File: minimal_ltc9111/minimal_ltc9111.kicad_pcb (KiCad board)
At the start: 4 copper layers, 62.2 x 19 mm, 35 parts, among them J1 FW-02-03-G-D-085-155, J2 FW-02-03-G-D-085-155, Q1 100 V, Q2 100 V, Q3 100 V, Q4 100.0 V, U1 LTC9111RDE-PBF

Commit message: Update subproject commit and correct component values in minimal_ltc9111.kicad_sch
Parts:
- L1: value 68 µH -> 68.0 µH

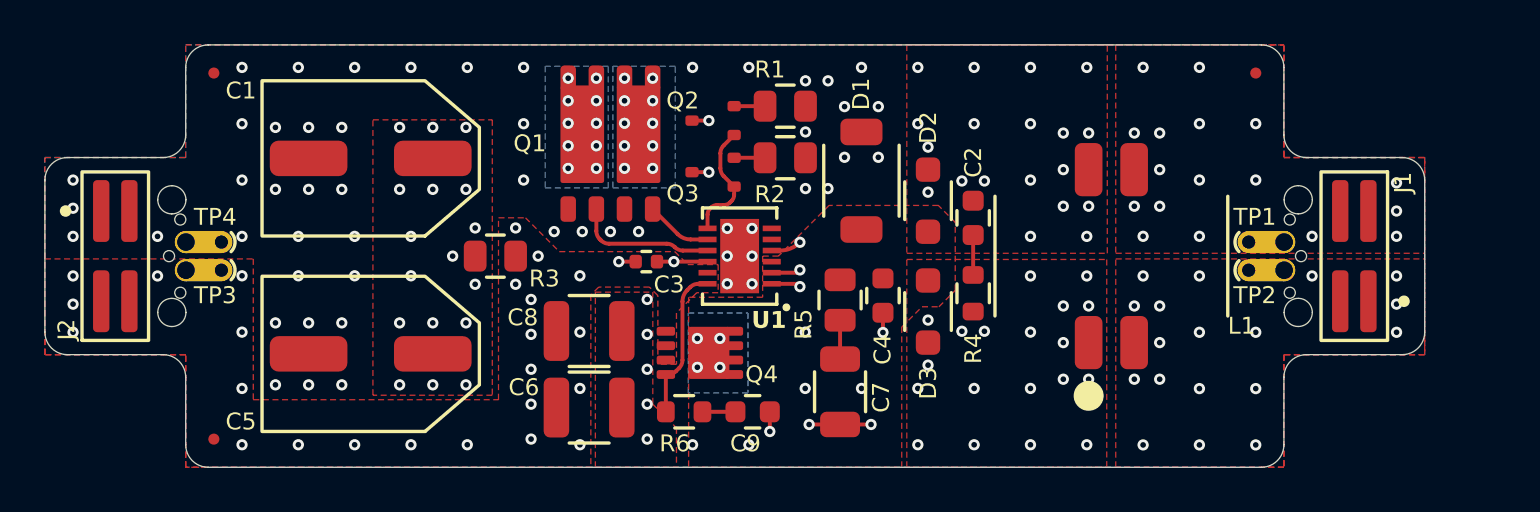
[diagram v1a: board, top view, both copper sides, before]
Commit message: Update subproject commit in KiCAD_Symbol_Generator
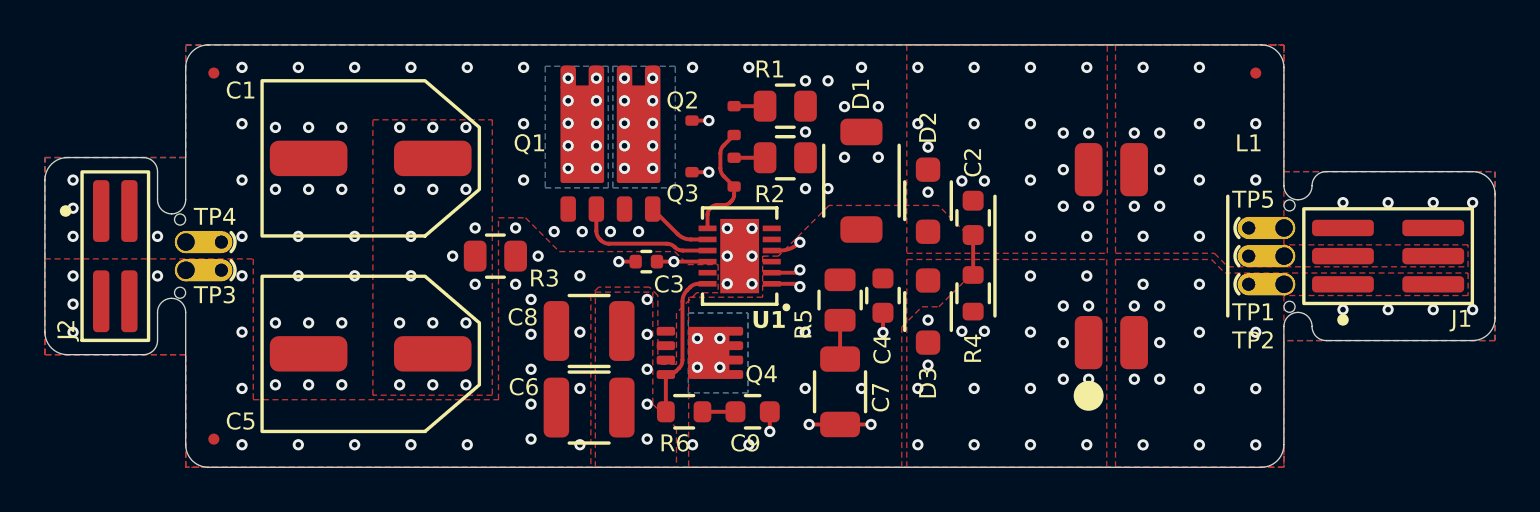
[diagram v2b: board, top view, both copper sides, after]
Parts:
- added TP5: TestPoint, test_point_footprints:TestPoint_THTPad_Castelated, F.Cu at (179.1, 103.9)
- J1: value FW-02-03-G-D-085-155 -> FW-03-03-G-D-085-155; footprint connector_footprints:FW-02-03-G-D-085-155 -> connector_footprints:FW-03-03-G-D-085-155
- MB1: footprint mouse_bite_footprints:mouse-bite-midle-50mil-200mil -> mouse_bite_footprints:mouse-bite-midle-50mil-250mil
- moved J1 1.52 mm to (183.8, 105.2), turned to 90 degrees
- moved TP1 0.64 mm to (179.1, 105.2)
- moved TP2 0.64 mm to (179.1, 106.4)
- turned MB1 to 90 degrees
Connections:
- J1 pad 2: /POWER_IN_P -> /POWER_IN_N
- J1 pad 3: /POWER_IN_N -> /POWER_IN_P
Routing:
- net GND: vias 68 -> 76
- net /POWER_IN_P: vias 17 -> 13
- net /POWER_IN_N: vias 18 -> 14
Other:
- board size 62.2 x 19 mm -> 65.4 x 19 mm

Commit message: Update footprint library URIs to reference KiCAD_Symbols_Generator
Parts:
- R1, R2, R3: value 3.3 -> 3.3 Ω
